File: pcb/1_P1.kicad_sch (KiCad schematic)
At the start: 17 parts, among them CON1 MIKROBUS_HOST_CONN, SW1 TS-1187A-B-A-B, SW2 TS-1187A-B-A-B, U1 ESP32-WROOM-32UE-N4, X1 50MHz

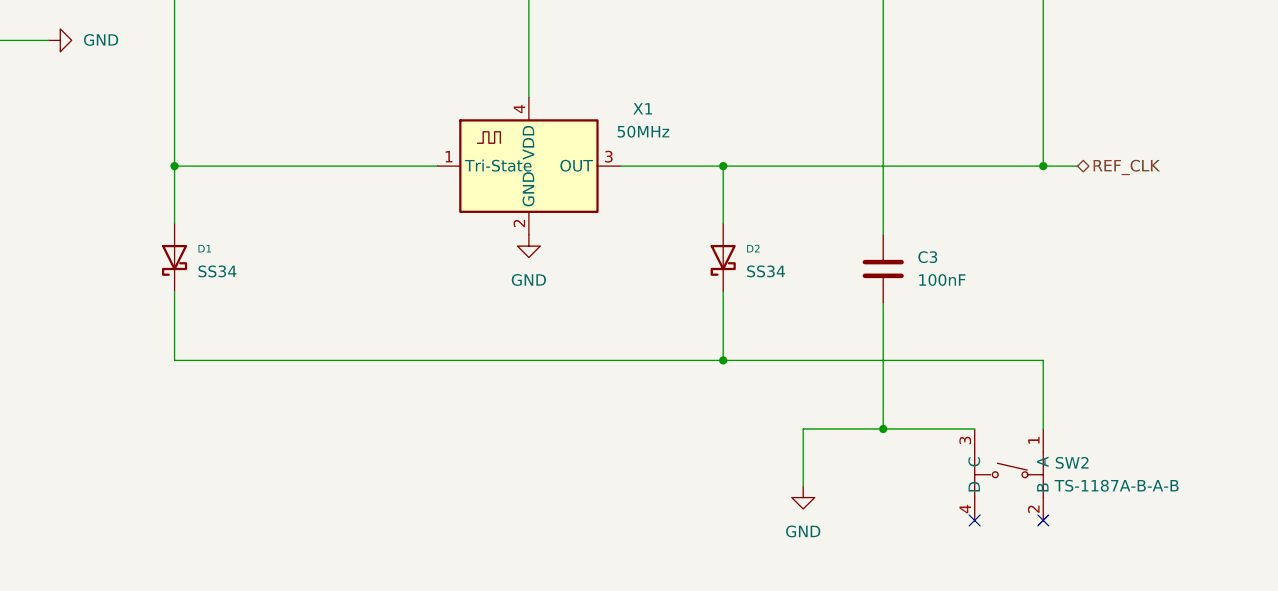
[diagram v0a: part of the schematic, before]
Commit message: 4 layer pcb
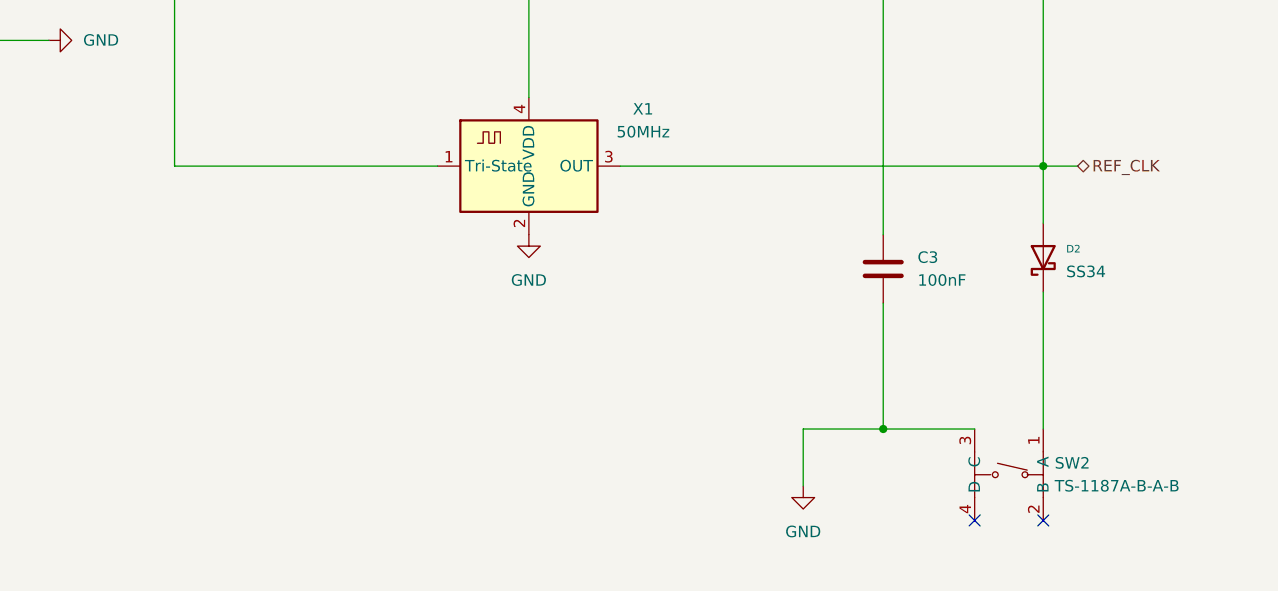
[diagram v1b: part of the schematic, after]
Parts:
- removed D1: SS34, Diode_SMD:D_SMA, symbol Diode:SS34
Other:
- moved on the sheet: D2
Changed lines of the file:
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@@
-	)
-	(junction
-		(at 227.33 137.16)
-		(diameter 0)
-		(color 0 0 0 0)
 	)
 	(junction
@@
 	)
 	(junction
-		(at 166.37 137.16)
-		(diameter 0)
-		(color 0 0 0 0)
-	)
-	(junction
 		(at 205.74 115.57)
-		(diameter 0)
-		(color 0 0 0 0)
-	)
-	(junction
-		(at 227.33 158.75)
 		(diameter 0)
 		(color 0 0 0 0)
@@
 	(wire
 		(pts
-			(xy 227.33 158.75) (xy 262.89 158.75)
-		)
-		(stroke
-			(width 0)
-			(type default)
-		)
-	)
-	(wire
-		(pts
 			(xy 77.47 137.16) (xy 87.63 137.16)
 		)
@@
 	(wire
 		(pts
-			(xy 166.37 158.75) (xy 227.33 158.75)
-		)
-		(stroke
-			(width 0)
-			(type default)
-		)
-	)
-	(wire
-		(pts
 			(xy 367.03 62.23) (xy 375.92 62.23)
 		)
@@
 	(wire
 		(pts
-			(xy 227.33 137.16) (xy 262.89 137.16)
-		)
-		(stroke
-			(width 0)
-			(type default)
-		)
-	)
-	(wire
-		(pts
 			(xy 152.4 123.19) (xy 146.05 123.19)
 		)
@@
 	(wire
 		(pts
-			(xy 227.33 137.16) (xy 227.33 143.51)
+			(xy 262.89 137.16) (xy 262.89 143.51)
 		)
 		(stroke
@@
 	(wire
 		(pts
-			(xy 215.9 137.16) (xy 227.33 137.16)
+			(xy 215.9 137.16) (xy 262.89 137.16)
 		)
 		(stroke
@@
 	(wire
 		(pts
-			(xy 166.37 151.13) (xy 166.37 158.75)
-		)
-		(stroke
-			(width 0)
-			(type default)
-		)
-	)
-	(wire
-		(pts
 			(xy 262.89 137.16) (xy 262.89 115.57)
 		)
@@
 	(wire
 		(pts
-			(xy 262.89 166.37) (xy 262.89 158.75)
+			(xy 262.89 151.13) (xy 262.89 166.37)
 		)
 		(stroke
@@
 	(wire
 		(pts
-			(xy 166.37 137.16) (xy 166.37 143.51)
-		)
-		(stroke
-			(width 0)
-			(type default)
-		)
-	)
-	(wire
-		(pts
 			(xy 146.05 115.57) (xy 166.37 115.57)
 		)
@@
 		(pts
 			(xy 60.96 151.13) (xy 26.67 151.13)
-		)
-		(stroke
-			(width 0)
-			(type default)
-		)
-	)
-	(wire
-		(pts
-			(xy 227.33 158.75) (xy 227.33 151.13)
 		)
 		(stroke
@@
 			)
 			(justify right)
-		)
-	)
-	(symbol
-		(lib_name "SS34_1")
-		(lib_id "Diode:SS34")
-		(at 166.37 147.32 90)
-		(unit 1)
-		(exclude_from_sim no)
-		(in_bom yes)
-		(on_board yes)
-		(dnp no)
-		(fields_autoplaced yes)
-		(property "Reference" "D1"
-			(at 168.91 146.3674 90)
-			(effects
-				(font
-					(size 0.8382 0.8382)
-				)
-				(justify right)
-			)
-		)
-		(property "Value" "SS34"
-			(at 168.91 148.9074 90)
-			(effects
-				(font
-					(size 1.27 1.27)
-				)
-				(justify right)
-			)
-		)
-		(property "Footprint" "Diode_SMD:D_SMA"
-			(at 170.815 147.32 0)
-			(effects
-				(font
-					(size 1.27 1.27)
-				)
-				(hide yes)
-			)
-		)
-		(property "Datasheet" "https://www.vishay.com/docs/88751/ss32.pdf"
-			(at 166.37 147.32 0)
-			(effects
-				(font
-					(size 1.27 1.27)
-				)
-				(hide yes)
-			)
-		)
-		(property "Description" "40V 3A Schottky Diode, SMA"
-			(at 166.37 147.32 0)
-			(effects
-				(font
-					(size 1.27 1.27)
-				)
-				(hide yes)
-			)
-		)
-		(property "LCSC" "C8678"
-			(at 162.56 147.32 0)
-			(effects
-				(font
-					(size 1.27 1.27)
-				)
-				(hide yes)
-			)
-		)
-		(pin "1"
-		)
-		(pin "2"
-		)
-		(instances
-			(project "Lichtstab"
-				(path "/e085f17c-3357-4281-ab9e-eebcecacdfc5/716186ee-16a1-4ec1-90c7-dc14427dfd17"
-					(reference "D1")
-					(unit 1)
-				)
-			)
 		)
 	)
@@
 		(lib_name "SS34_1")
 		(lib_id "Diode:SS34")
-		(at 227.33 147.32 90)
+		(at 262.89 147.32 90)
 		(unit 1)
 		(exclude_from_sim no)
@@
 		(fields_autoplaced yes)
 		(property "Reference" "D2"
-			(at 229.87 146.3674 90)
+			(at 265.43 146.3674 90)
 			(effects
 				(font
@@
 		)
 		(property "Value" "SS34"
-			(at 229.87 148.9074 90)
+			(at 265.43 148.9074 90)
 			(effects
 				(font
@@
 		)
 		(property "Footprint" "Diode_SMD:D_SMA"
-			(at 231.775 147.32 0)
+			(at 267.335 147.32 0)
 			(effects
 				(font
@@
 		)
 		(property "Datasheet" "https://www.vishay.com/docs/88751/ss32.pdf"
-			(at 227.33 147.32 0)
+			(at 262.89 147.32 0)
 			(effects
 				(font
@@
 		)
 		(property "Description" "40V 3A Schottky Diode, SMA"
-			(at 227.33 147.32 0)
+			(at 262.89 147.32 0)
 			(effects
 				(font
@@
 		)
 		(property "LCSC" "C8678"
-			(at 223.52 147.32 0)
-			(effects
-				(font
+			(at 259.08 147.32 0)
+			(effects
+				(font

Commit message: review version
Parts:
- C1: footprint Capacitor_SMD:C_0805_2012Metric -> Capacitor_SMD:C_1206_3216Metric; LCSC (none) -> C22367835

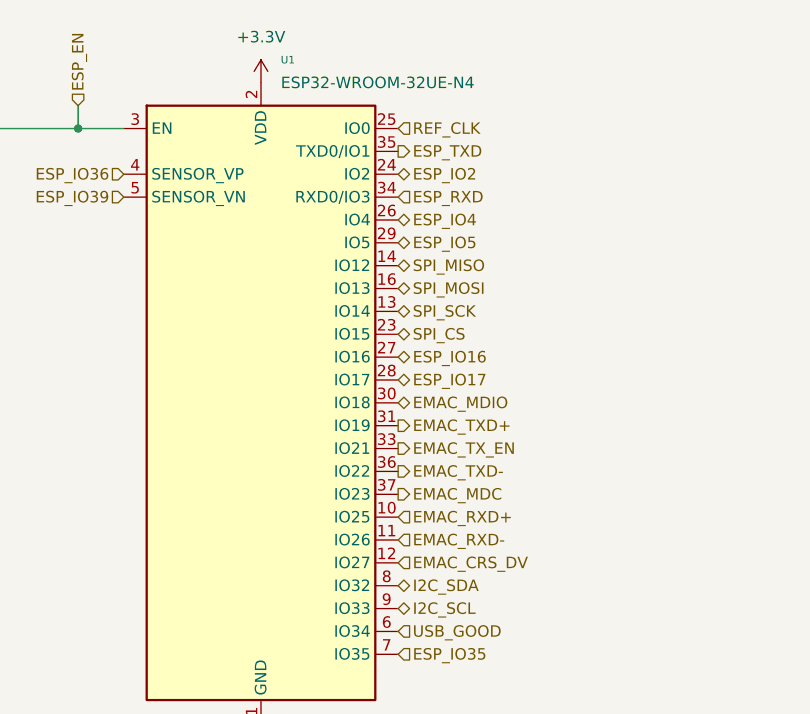
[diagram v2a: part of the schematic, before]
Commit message: remove third pcb and more flash
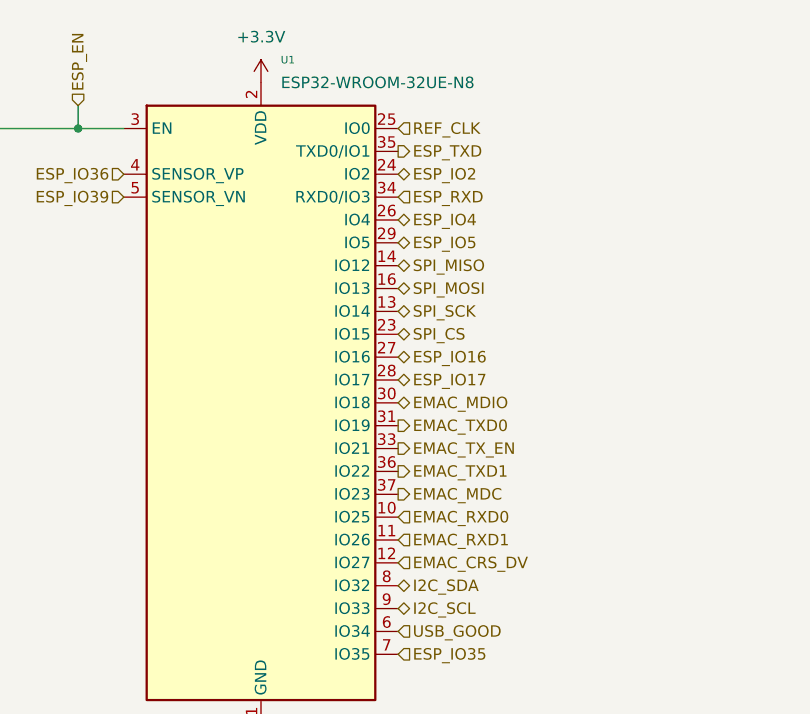
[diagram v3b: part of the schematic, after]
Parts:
- U1: value ESP32-WROOM-32UE-N4 -> ESP32-WROOM-32UE-N8; LCSC C701344 -> C701345
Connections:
- net EMAC_RXD+ renamed EMAC_RXD0
- net EMAC_RXD- renamed EMAC_RXD1
- net EMAC_TXD+ renamed EMAC_TXD0
- net EMAC_TXD- renamed EMAC_TXD1
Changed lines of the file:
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@@
 		)
 	)
-	(hierarchical_label "EMAC_TXD-"
+	(hierarchical_label "EMAC_TXD1"
 		(shape output)
 		(at 234.95 67.31 0)
@@
 		)
 	)
-	(hierarchical_label "EMAC_RXD+"
+	(hierarchical_label "EMAC_RXD0"
 		(shape input)
 		(at 234.95 72.39 0)
@@
 		)
 	)
-	(hierarchical_label "EMAC_TXD+"
+	(hierarchical_label "EMAC_TXD0"
 		(shape output)
 		(at 234.95 62.23 0)
@@
 		)
 	)
-	(hierarchical_label "EMAC_RXD-"
+	(hierarchical_label "EMAC_RXD1"
 		(shape input)
 		(at 234.95 74.93 0)
@@
 			)
 		)
-		(property "Value" "ESP32-WROOM-32UE-N4"
+		(property "Value" "ESP32-WROOM-32UE-N8"
 			(at 221.9041 24.13 0)
 			(effects
@@
 			)
 		)
-		(property "LCSC" "C701344"
+		(property "LCSC" "C701345"
 			(at 207.01 86.36 0)
 			(effects
